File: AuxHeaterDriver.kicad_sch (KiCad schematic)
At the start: 1 part

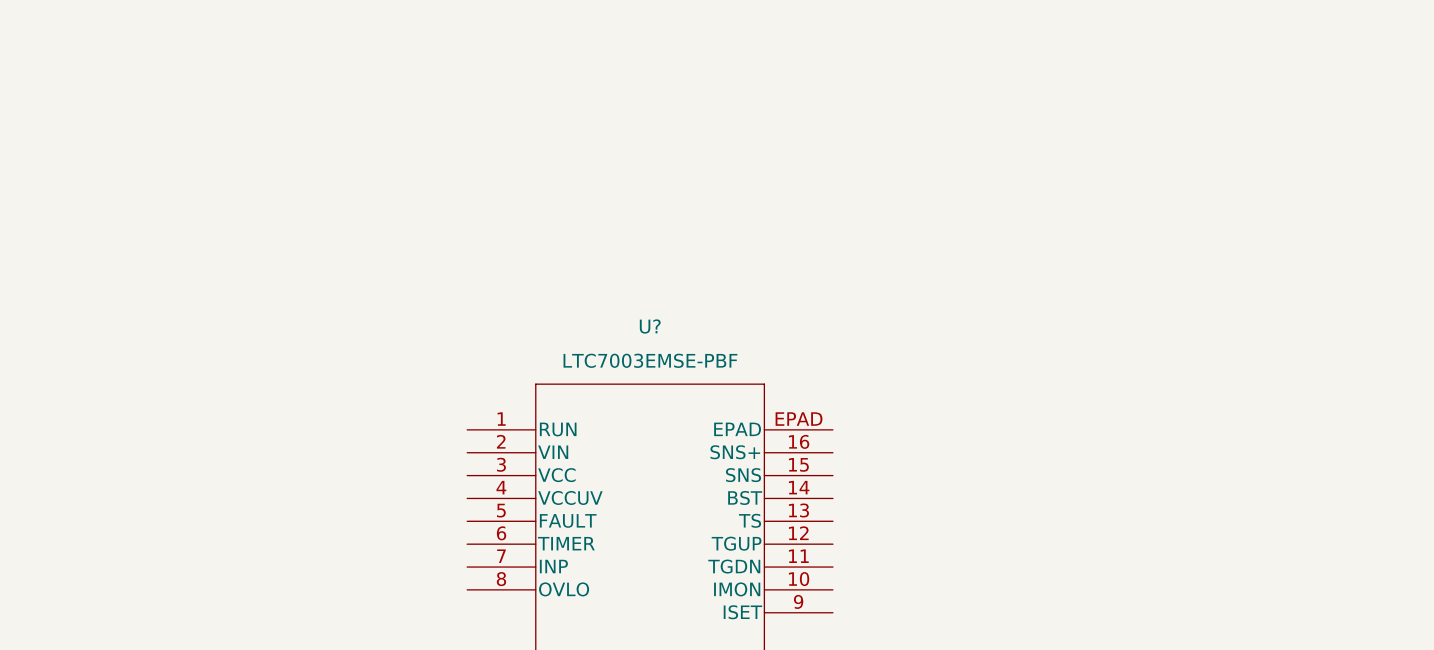
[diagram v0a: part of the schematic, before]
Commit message: add sys and spare connectors
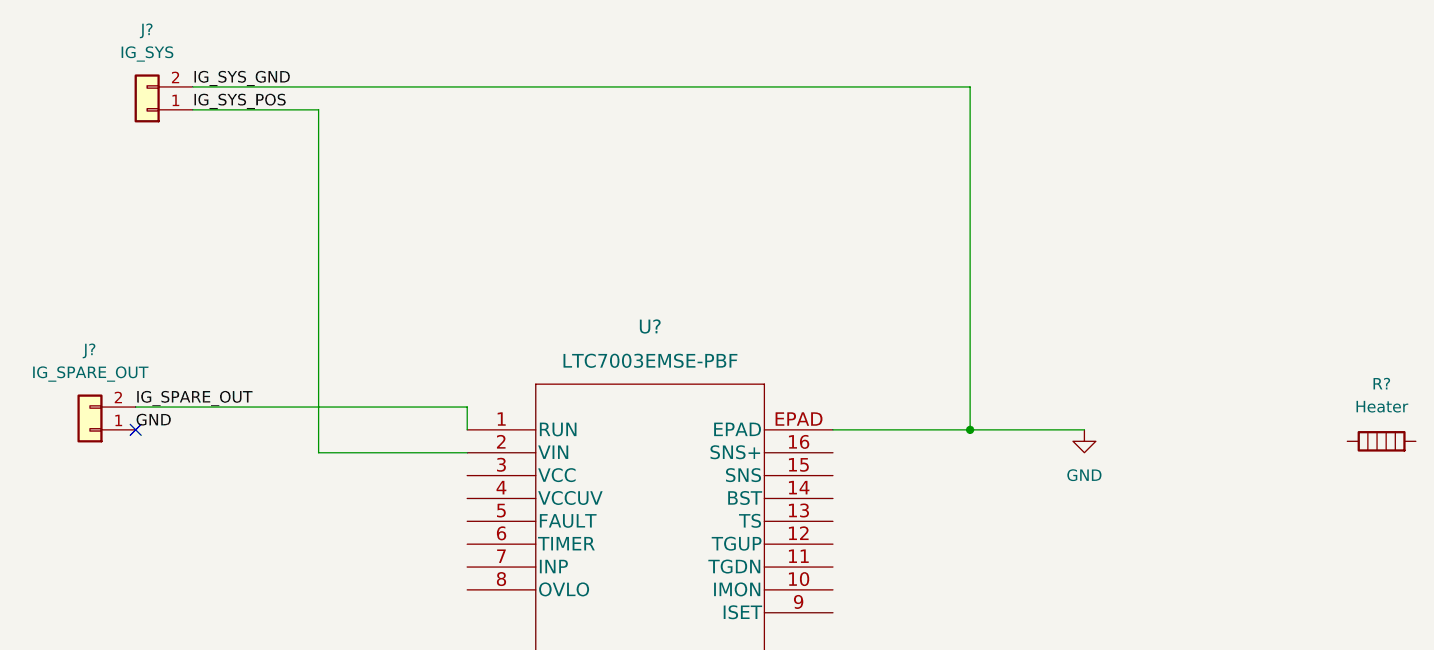
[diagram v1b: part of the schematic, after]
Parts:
- added J?: IG_SYS, symbol Connector_Generic:Conn_01x02
- added J?: IG_SPARE_OUT, symbol Connector_Generic:Conn_01x02
- added R?: Heater, symbol Device:Heater
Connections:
- net IG_SPARE_OUT: now reaches U?.1 (RUN)
- net IG_SPARE_OUT: now also J?.2 (Pin_2)
- net IG_SYS_POS: now reaches U?.2 (VIN)
- net IG_SYS_POS: now also J?.1 (Pin_1)
- net GND: now reaches U?.EPAD
- net GND: now also J?.1 (Pin_1), J?.2 (Pin_2)
- no-connect marks 0 -> 1
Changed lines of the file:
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@@
 (kicad_sch (version 20211123) (generator eeschema)
   (paper "A4")
+  (junction (at 181.61 78.74) (diameter 0) (color 0 0 0 0)
+  )
+  (no_connect (at 88.9 78.74))
+  (wire (pts (xy 109.22 81.28) (xy 125.73 81.28))
+    (stroke (width 0) (type default) (color 0 0 0 0))
+  )
+  (wire (pts (xy 95.25 43.18) (xy 109.22 43.18))
+    (stroke (width 0) (type default) (color 0 0 0 0))
+  )
+  (wire (pts (xy 88.9 76.2) (xy 125.73 76.2))
+    (stroke (width 0) (type default) (color 0 0 0 0))
+  )
+  (wire (pts (xy 109.22 43.18) (xy 109.22 81.28))
+    (stroke (width 0) (type default) (color 0 0 0 0))
+  )
+  (wire (pts (xy 125.73 76.2) (xy 125.73 78.74))
+    (stroke (width 0) (type default) (color 0 0 0 0))
+  )
+  (wire (pts (xy 181.61 78.74) (xy 194.31 78.74))
+    (stroke (width 0) (type default) (color 0 0 0 0))
+  )
+  (wire (pts (xy 181.61 40.64) (xy 181.61 78.74))
+    (stroke (width 0) (type default) (color 0 0 0 0))
+  )
+  (wire (pts (xy 166.37 78.74) (xy 181.61 78.74))
+    (stroke (width 0) (type default) (color 0 0 0 0))
+  )
+  (wire (pts (xy 95.25 40.64) (xy 181.61 40.64))
+    (stroke (width 0) (type default) (color 0 0 0 0))
+  )
+  (label "IG_SPARE_OUT" (at 88.9 76.2 0)
+    (effects (font (size 1.27 1.27)) (justify left bottom))
+  )
+  (label "IG_SYS_GND" (at 95.25 40.64 0)
+    (effects (font (size 1.27 1.27)) (justify left bottom))
+  )
+  (label "GND" (at 88.9 78.74 0)
+    (effects (font (size 1.27 1.27)) (justify left bottom))
+  )
+  (label "IG_SYS_POS" (at 95.25 43.18 0)
+    (effects (font (size 1.27 1.27)) (justify left bottom))
+  )
+  (symbol (lib_id "Connector_Generic:Conn_01x02") (at 90.17 43.18 180) (unit 1)
+    (in_bom yes) (on_board yes) (fields_autoplaced)
+    (property "Reference" "J?" (id 0) (at 90.17 34.29 0))
+    (property "Value" "IG_SYS" (id 1) (at 90.17 36.83 0))
+    (property "Footprint" "" (id 2) (at 90.17 43.18 0)
+      (effects (font (size 1.27 1.27)) hide)
+    )
+    (property "Datasheet" "~" (id 3) (at 90.17 43.18 0)
+      (effects (font (size 1.27 1.27)) hide)
+    )
+    (pin "1")
+    (pin "2")
+  )
+  (symbol (lib_id "Device:Heater") (at 227.33 80.01 90) (unit 1)
+    (in_bom yes) (on_board yes) (fields_autoplaced)
+    (property "Reference" "R?" (id 0) (at 227.33 73.66 90))
+    (property "Value" "Heater" (id 1) (at 227.33 76.2 90))
+    (property "Footprint" "" (id 2) (at 227.33 81.788 90)
+      (effects (font (size 1.27 1.27)) hide)
+    )
+    (property "Datasheet" "~" (id 3) (at 227.33 80.01 0)
+      (effects (font (size 1.27 1.27)) hide)
+    )
+    (pin "1")
+    (pin "2")
+  )
+  (symbol (lib_id "Connector_Generic:Conn_01x02") (at 83.82 78.74 180) (unit 1)
+    (in_bom yes) (on_board yes) (fields_autoplaced)
+    (property "Reference" "J?" (id 0) (at 83.82 69.85 0))
+    (property "Value" "IG_SPARE_OUT" (id 1) (at 83.82 72.39 0))
+    (property "Footprint" "" (id 2) (at 83.82 78.74 0)
+      (effects (font (size 1.27 1.27)) hide)
+    )
+    (property "Datasheet" "~" (id 3) (at 83.82 78.74 0)
+      (effects (font (size 1.27 1.27)) hide)
+    )
+    (pin "1")
+    (pin "2")
+  )
+  (symbol (lib_id "power:GND") (at 194.31 78.74 0) (unit 1)
+    (in_bom yes) (on_board yes) (fields_autoplaced)
+    (property "Reference" "#PWR?" (id 0) (at 194.31 85.09 0)
+      (effects (font (size 1.27 1.27)) hide)
+    )
+    (property "Value" "GND" (id 1) (at 194.31 83.82 0))
+    (property "Footprint" "" (id 2) (at 194.31 78.74 0)
+      (effects (font (size 1.27 1.27)) hide)
+    )
+    (property "Datasheet" "" (id 3) (at 194.31 78.74 0)
+      (effects (font (size 1.27 1.27)) hide)
+    )
+    (pin "1")
+  )
   (symbol (lib_id "AuxHeaterDriver:LTC7003EMSE-PBF") (at 125.73 78.74 0) (unit 1)
     (in_bom yes) (on_board yes) (fields_autoplaced)
@@
   )
   (symbol_instances
+    (path "/f0ba2953-0bcf-4b83-9822-f15b76064a05"
+      (reference "#PWR?") (unit 1) (value "GND") (footprint "")
+    )
+    (path "/6ed196e0-51c4-48e3-bf8e-f96bd3bbf776"
+      (reference "J?") (unit 1) (value "IG_SYS") (footprint "")
+    )
+    (path "/d5d90caa-3f7d-4bdf-aa08-89540201f8bb"
+      (reference "J?") (unit 1) (value "IG_SPARE_OUT") (footprint "")
+    )
+    (path "/aa2c6ad6-36ef-4e64-b349-b1fbea8891c3"
+      (reference "R?") (unit 1) (value "Heater") (footprint "")
+    )
     (path "/f8da869a-dfd7-4a06-af04-87bf62d4057a"
       (reference "U?") (unit 1) (value "LTC7003EMSE-PBF") (footprint "MSE_16_ADI")

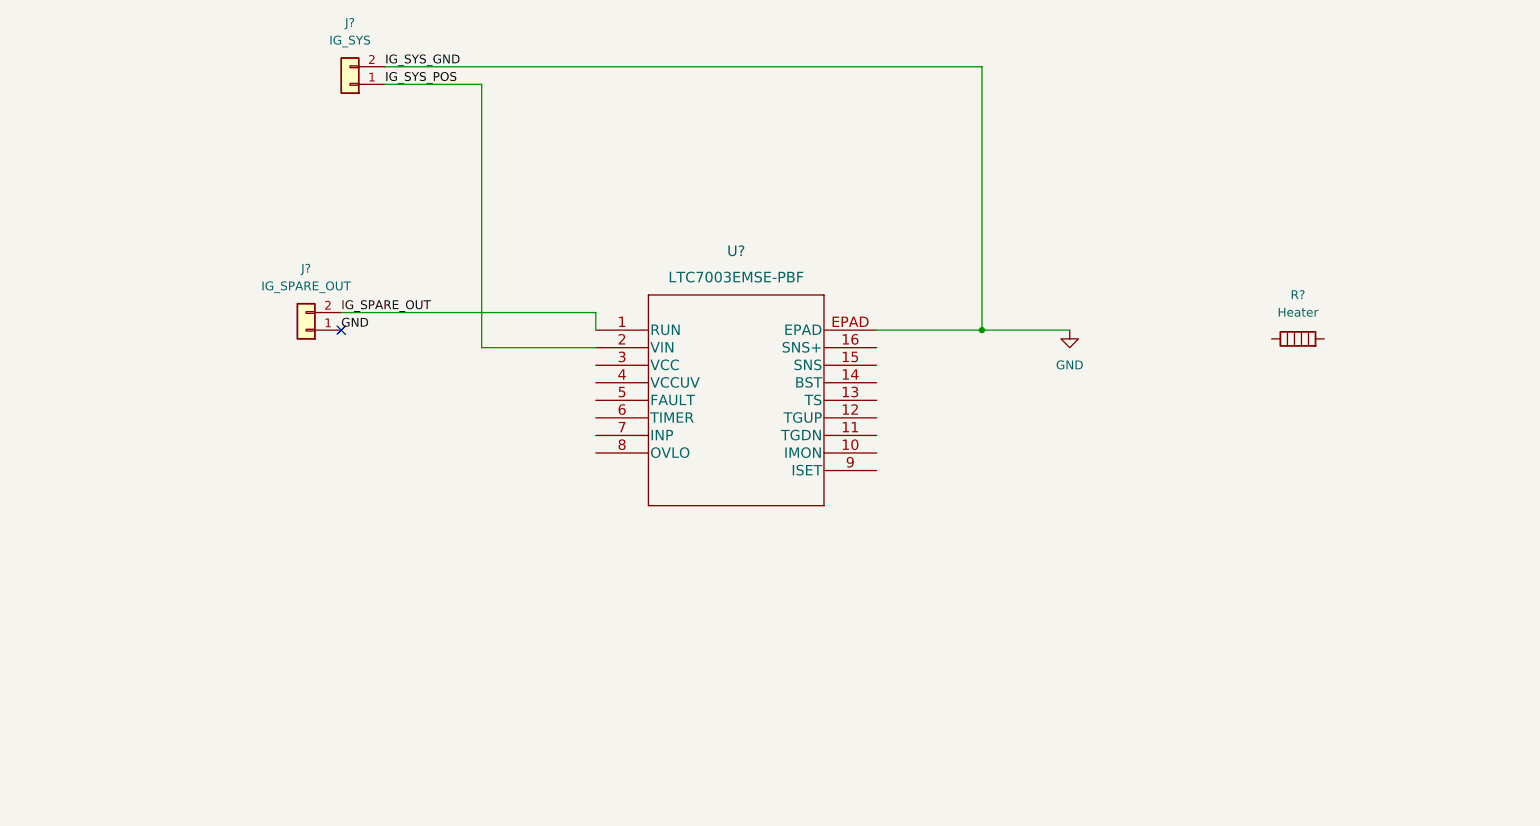
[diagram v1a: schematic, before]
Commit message: initial stab at connecting up the smart switch
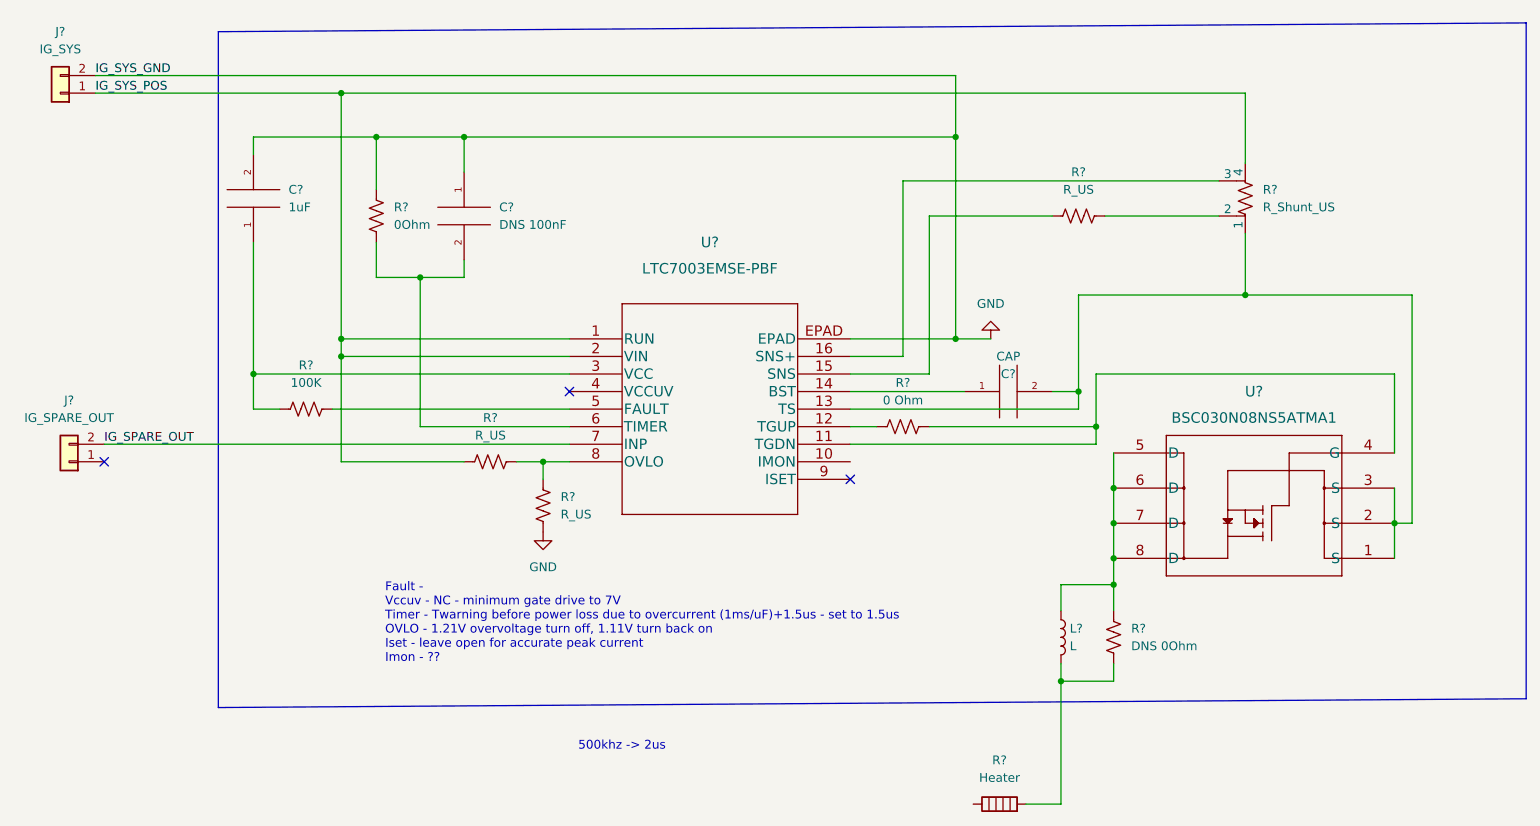
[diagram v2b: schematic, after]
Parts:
- added C?: 1uF, symbol pspice:CAP
- added C?: DNS 100nF, symbol pspice:CAP
- added C?: CAP, symbol pspice:CAP
- added L?: L, symbol Device:L
- added R?: 100K, symbol Device:R_US
- added R? (x3): R_US, symbol Device:R_US
- added R?: 0Ohm, symbol Device:R_US
- added R?: DNS 0Ohm, symbol Device:R_US
- added R?: R_Shunt_US, symbol Device:R_Shunt_US
- added R?: 0 Ohm, symbol Device:R_US
- added U?: BSC030N08NS5ATMA1, QFN8_BSC030N08NS5ATMA1_INF, symbol AuxHeaterDriver:BSC030N08NS5ATMA1
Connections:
- net GND: now also C?.1, C?.2, R?.1, R?.2; no longer J?.1 (Pin_1)
- net IG_SPARE_OUT: now also U?.7 (INP); no longer U?.1 (RUN)
- net IG_SYS_POS: now also U?.1 (RUN), R?.2, R?.4
- net at R?.2: now also L?.2, R?.2
- net at U?.11 (TGDN): now also R?.2, U?.4 (G)
- net at U?.12 (TGUP): now also R?.1
- net at U?.13 (TS): now also C?.2, R?.1, U?.1 (S), U?.2 (S), U?.3 (S)
- net at U?.14 (BST): now also C?.1
- net at U?.15 (SNS): now also R?.1
- net at U?.16 (SNS+): now also R?.3
- net at U?.3 (VCC): now also C?.1, R?.2
- net at U?.5 (FAULT): now also R?.1
- net at U?.6 (TIMER): now also C?.2, R?.2
- net at U?.8 (OVLO): now also R?.1, R?.1
- new net: L?.1, R?.1, U?.5 (D), U?.6 (D), U?.7 (D), U?.8 (D)
- new net: R?.2, R?.2
- no-connect marks 1 -> 3
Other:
- note added: "500khz -> 2us"
- note added: "Fault - Vccuv - NC - minimum gate drive to 7V Timer - Twarning before power loss due to overcurrent (1ms/uF)+1.5us - set to 1.5us OVLO - 1.21V overvoltage turn off, 1.11V turn back on Iset - leave open for accurate peak current Imon - ??"
- moved on the sheet: J?, R?, U?
